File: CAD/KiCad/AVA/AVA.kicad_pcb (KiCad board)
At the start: 2 copper layers, 100 x 75 mm, 48 parts, among them J1 Conn_01x03_Pin, J10 Conn_01x04_Pin, J2 Conn_01x03_Pin, J3 Conn_01x03_Pin, J4 Conn_01x03_Pin, J5 Conn_01x02_Pin, J6 Conn_01x02_Pin, J7 Conn_01x02_Pin, J8 Conn_01x03_Pin, J9 Conn_01x03_Pin, U1 ESP32-C3-Super-Mini, U2 ESP32-DevKitC

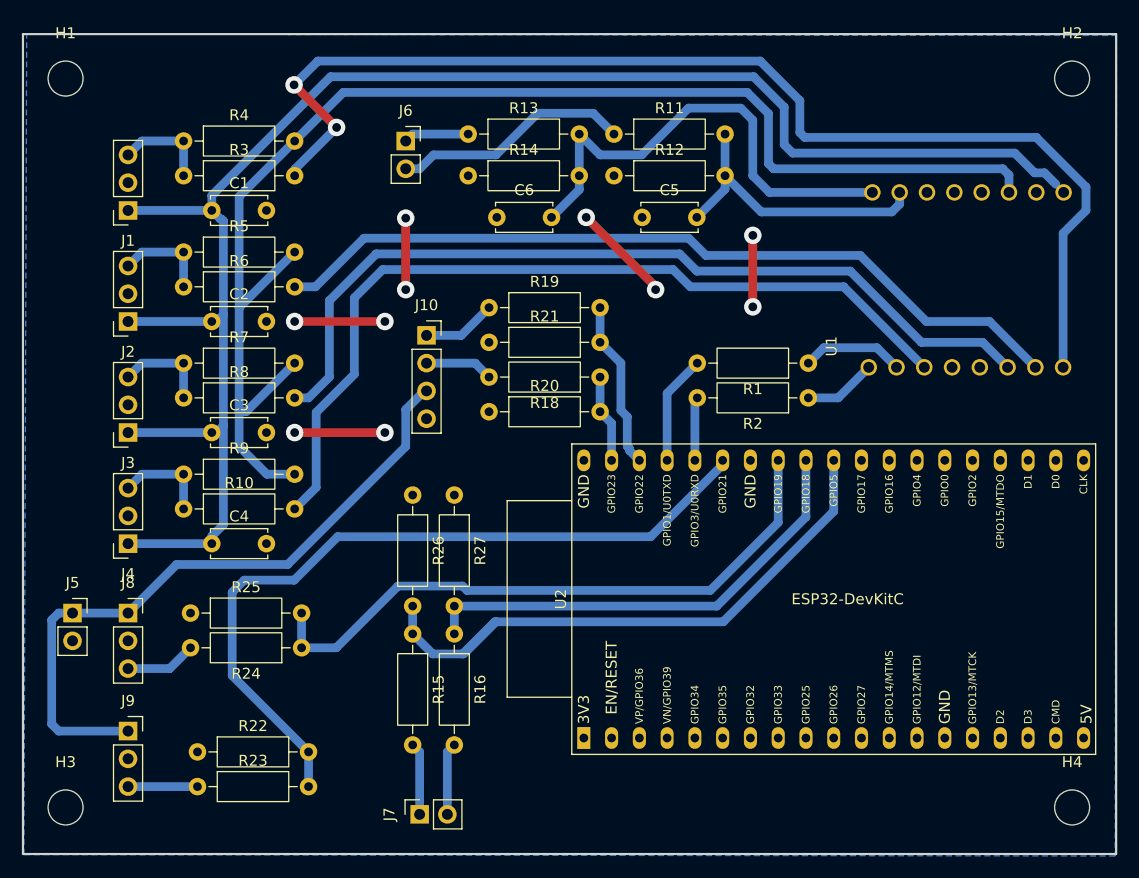
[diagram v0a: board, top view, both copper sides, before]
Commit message: SVG update for connectors
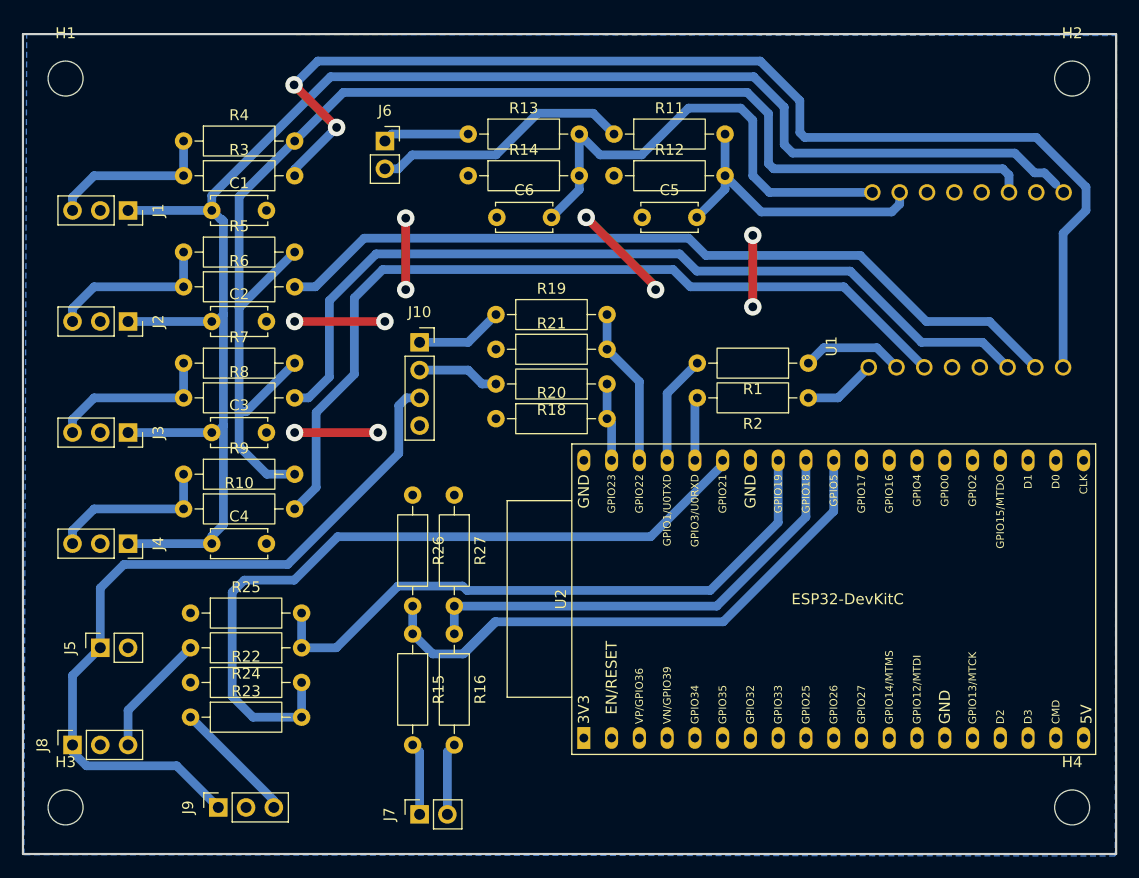
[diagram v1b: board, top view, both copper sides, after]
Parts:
- moved J8 13.1 mm to (131.4, 116.2), turned to 90 degrees
- moved J9 10.8 mm to (144.8, 121.9), turned to 90 degrees
- moved R22 6.38 mm to (142.2, 110.5)
- moved R23 6.38 mm to (142.2, 113.7)
- moved J5 4.07 mm to (134.0, 107.3), turned to 90 degrees
- moved J6 1.91 mm to (160.0, 61.0)
- moved J10 0.90 mm to (163.2, 79.4)
- moved R20 0.90 mm to (170.2, 86.4)
- moved R21 0.90 mm to (170.2, 80.0)
- moved R19 0.90 mm to (170.2, 76.8)
- moved R18 0.90 mm to (180.3, 83.2)
- turned J1 to -90 degrees
- turned J2 to -90 degrees
- turned J3 to -90 degrees
- turned J4 to -90 degrees
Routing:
- net /6.2V: track 61.7 -> 70.5 mm
- net Net-(J4-Pin_3): track 8.78 -> 15.4 mm
- net Net-(J1-Pin_3): track 8.78 -> 15.4 mm
- net Net-(J3-Pin_3): track 8.78 -> 15.4 mm
- net Net-(J2-Pin_3): track 8.78 -> 15.4 mm
- net /PWM-Motor: track 6.35 -> 11.4 mm
- net /PWM-Servo: track 6.50 -> 11.3 mm
- net /BAT2(8V): track 21.9 -> 23.8 mm
- net /BAT1(14V): track 5.98 -> 7.88 mm
- net /CH1: track 6.77 -> 8.04 mm
- net /CH2: track 6.24 -> 7.51 mm
- net Net-(U2-GPIO23): track 8.06 -> 7.16 mm
- net Net-(U2-GPIO22): track 15.5 -> 14.6 mm
- net Net-(U2-GPIO21): track 70.8 -> 69.9 mm
- net GND: track 38.8 -> 38.2 mm

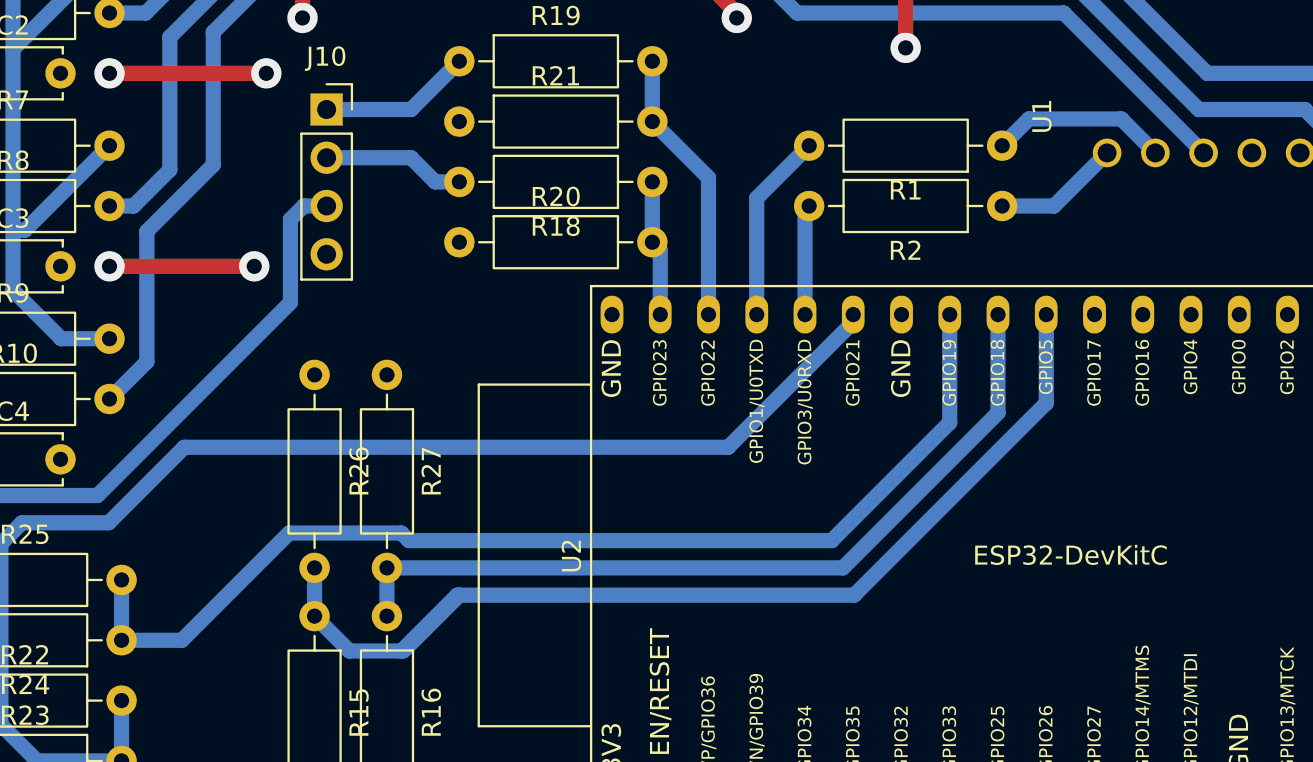
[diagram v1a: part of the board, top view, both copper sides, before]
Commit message: ESP32-DevKitC UART pins shared with usb, changing it to GPIO16/17. GPIO5 is strapping pin, changing pwm channels to GPIO4,18,19,20,21,22,23. GPIO4 in RTC-power-domain (touch sensor for deep-sleep mode, using it as normal PWM GPIO
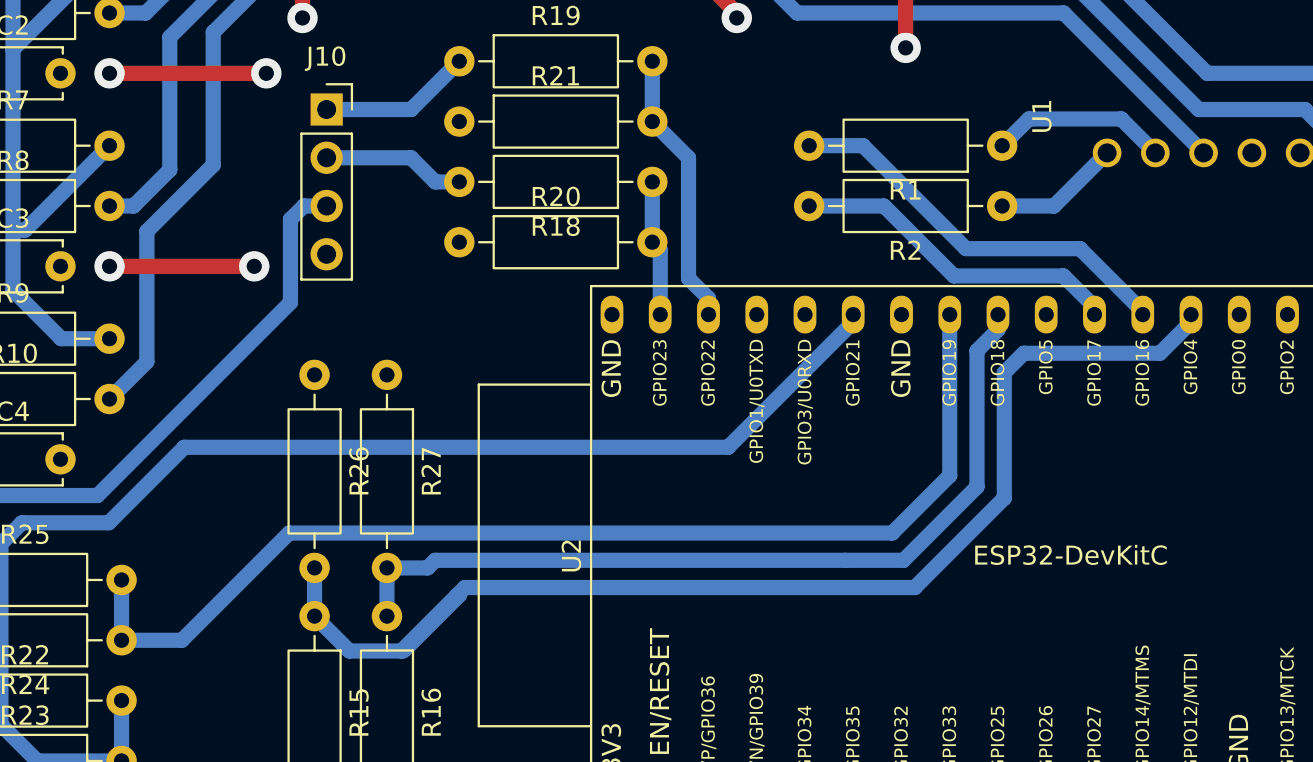
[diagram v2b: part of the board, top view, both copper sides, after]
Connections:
- R1 pad 2: Net-(U2-U0TXD/GPIO1) -> Net-(U2-GPIO16)
- R15 pad 1: Net-(U2-GPIO5) -> Net-(U2-ADC2_CH0/GPIO4)
- R2 pad 2: Net-(U2-U0RXD/GPIO3) -> Net-(U2-GPIO17)
- R26 pad 2: Net-(U2-GPIO5) -> Net-(U2-ADC2_CH0/GPIO4)
- U2 pad 26: unconnected-(U2-ADC2_CH0/GPIO4-Pad26) -> Net-(U2-ADC2_CH0/GPIO4)
- U2 pad 27: unconnected-(U2-GPIO16-Pad27) -> Net-(U2-GPIO16)
- U2 pad 28: unconnected-(U2-GPIO17-Pad28) -> Net-(U2-GPIO17)
- U2 pad 29: Net-(U2-GPIO5) -> unconnected-(U2-GPIO5-Pad29)
- U2 pad 34: Net-(U2-U0RXD/GPIO3) -> unconnected-(U2-U0RXD/GPIO3-Pad34)
- U2 pad 35: Net-(U2-U0TXD/GPIO1) -> unconnected-(U2-U0TXD/GPIO1-Pad35)
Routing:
- net Net-(U2-ADC2_CH0/GPIO4): track 0.00 -> 65.1 mm
- net Net-(U2-GPIO5): track 56.0 -> 0.00 mm
- net Net-(U2-GPIO16): track 0.00 -> 21.3 mm
- net Net-(U2-GPIO17): track 0.00 -> 17.6 mm
- net Net-(U2-U0TXD/GPIO1): track 10.0 -> 0.00 mm
- net Net-(U2-U0RXD/GPIO3): track 5.81 -> 0.00 mm
- net Net-(U2-GPIO18): track 43.3 -> 44.9 mm
- net Net-(U2-GPIO19): track 57.5 -> 58.8 mm

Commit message: Newest SVG, cropped. Footprints I'm flipping, my wrists I'm slitting
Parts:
- U1: moved to B.Cu
- moved R2 14.8 mm to (191.1, 71.8), turned to -90 degrees
- moved R1 10.5 mm to (194.3, 71.8), turned to -90 degrees
- moved U1 4.53 mm to (208.9, 74.5), turned to -90 degrees
- moved C5 2.62 mm to (182.9, 70.5)
- moved J6 2.62 mm to (160.7, 63.5)
- moved R11 2.62 mm to (180.3, 62.9)
- moved R12 2.62 mm to (180.3, 66.7)
- moved C6 2.54 mm to (170.3, 70.5)
- moved R13 2.54 mm to (167.6, 62.9)
- moved R14 2.54 mm to (167.6, 66.7)
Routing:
- net VCC: track 153.9 -> 206.0 mm
- net Net-(U1-3.3V): track 124.9 -> 175.7 mm
- net Net-(U1-PISO/GPIO5): track 108.7 -> 77.5 mm, vias 2 -> 0
- net GND: track 38.2 -> 24.8 mm, vias 10 -> 6
- net Net-(U1-GPIO10): track 78.5 -> 88.1 mm
- net Net-(U1-SS/GPIO7): track 79.1 -> 88.3 mm
- net Net-(U1-POSI/GPIO6): track 74.5 -> 82.0 mm
- net Net-(U1-TX/GPIO21): track 6.68 -> 12.0 mm
- net Net-(U2-GPIO16): track 21.3 -> 16.8 mm
- net Net-(U1-A1/GPIO1): track 27.4 -> 29.8 mm
- net Net-(U1-RX/GPIO20): track 9.39 -> 11.7 mm
- net Net-(U1-A0/GPIO0): track 44.2 -> 42.7 mm
- net /BAT2(8V): track 23.8 -> 22.9 mm
- net /BAT1(14V): track 7.88 -> 7.25 mm
- net Net-(U2-GPIO17): track 17.6 -> 17.1 mm

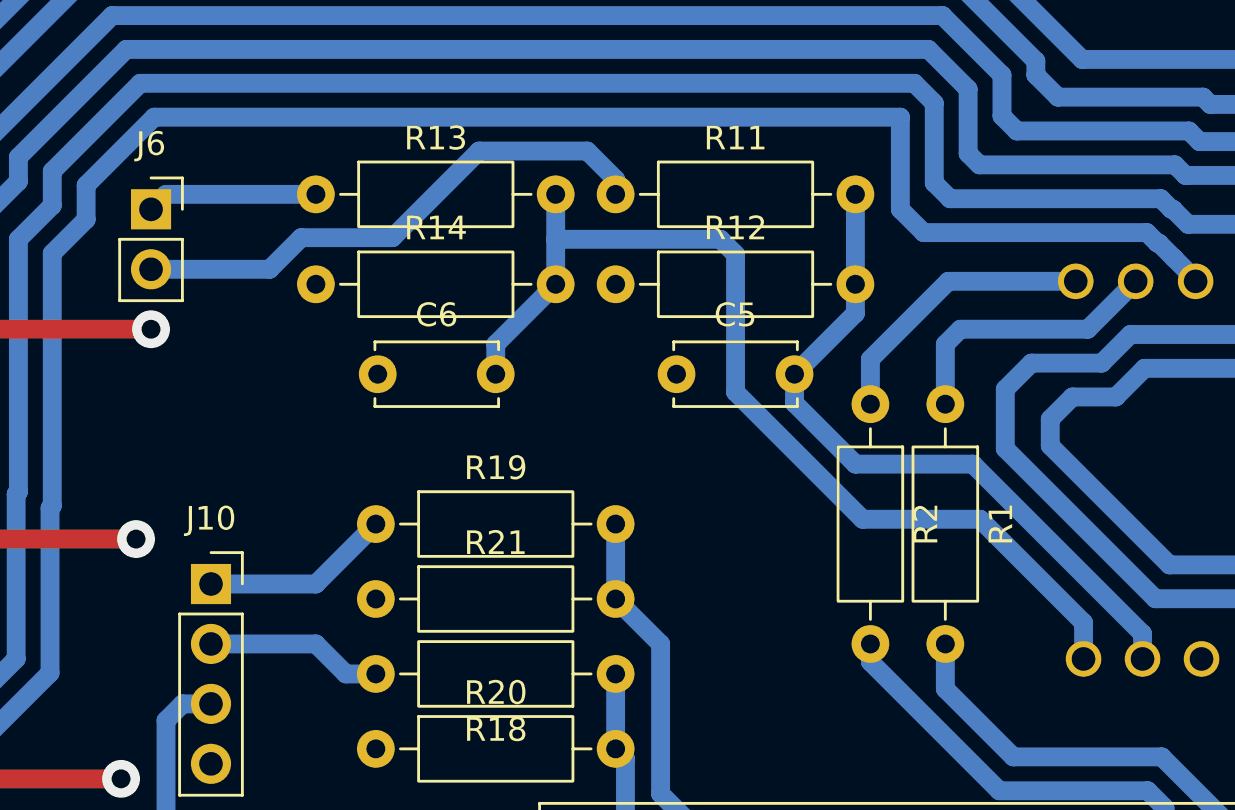
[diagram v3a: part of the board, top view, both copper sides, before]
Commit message: Removed copper islands from circuit
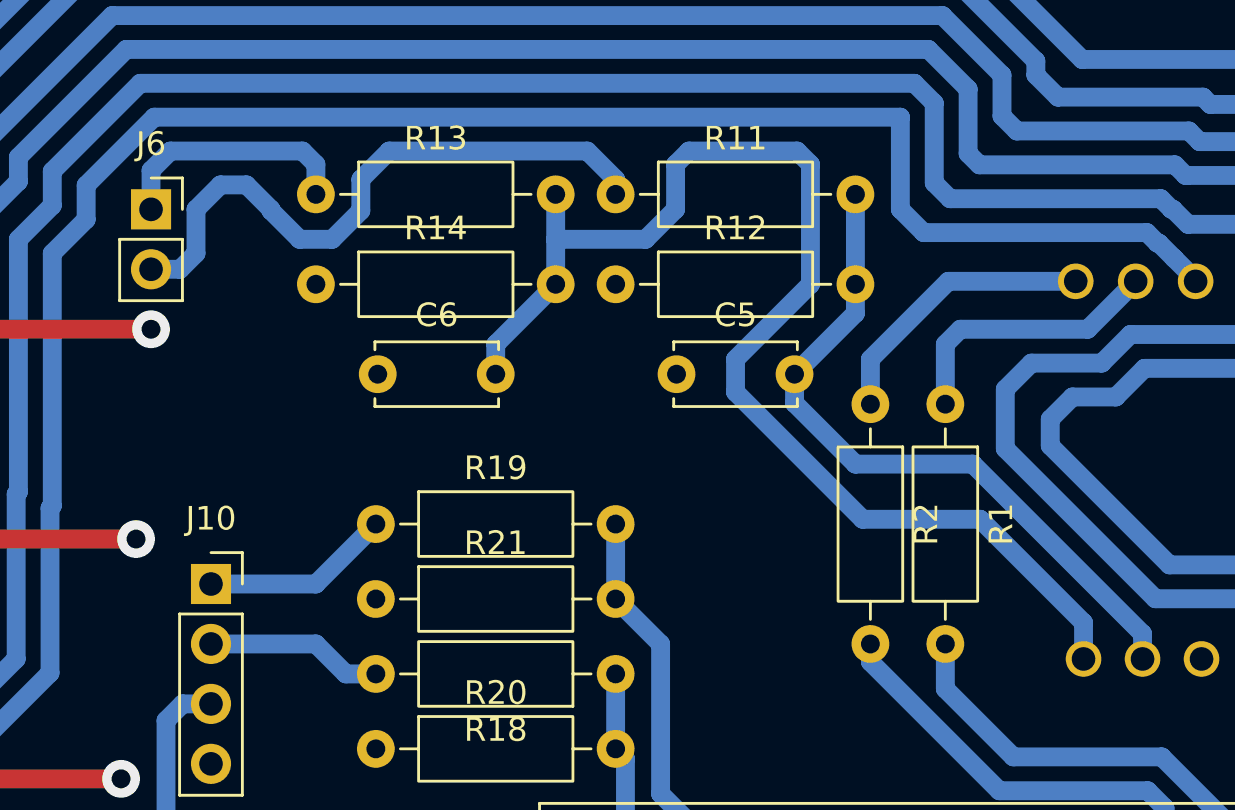
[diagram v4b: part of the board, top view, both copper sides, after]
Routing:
- net Net-(U1-A0/GPIO0): track 42.7 -> 53.7 mm
- net /BAT2(8V): track 22.9 -> 26.7 mm
- net /BAT1(14V): track 7.25 -> 10.5 mm
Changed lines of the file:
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@@
-	)
-	(segment
-		(start 184.785 64.77)
-		(end 177.8 64.77)
-		(width 0.8)
-		(layer "B.Cu")
-		(net "Net-(U1-A0{slash}GPIO0)")
 	)
 	(segment
 		(start 190.807143 76.631539)
+		(end 195.78346 76.631539)
+		(width 0.8)
+		(layer "B.Cu")
+		(net "Net-(U1-A0{slash}GPIO0)")
+	)
+	(segment
+		(start 188.595 66.675)
+		(end 185.42 69.85)
+		(width 0.8)
+		(layer "B.Cu")
+		(net "Net-(U1-A0{slash}GPIO0)")
+	)
+	(segment
+		(start 183.445 61.03)
+		(end 188.03 61.03)
+		(width 0.8)
+		(layer "B.Cu")
+		(net "Net-(U1-A0{slash}GPIO0)")
+	)
+	(segment
+		(start 185.42 69.85)
 		(end 185.42 71.244396)
-		(width 0.8)
-		(layer "B.Cu")
-		(net "Net-(U1-A0{slash}GPIO0)")
-	)
-	(segment
-		(start 185.42 71.244396)
-		(end 185.42 65.405)
-		(width 0.8)
-		(layer "B.Cu")
-		(net "Net-(U1-A0{slash}GPIO0)")
-	)
-	(segment
-		(start 195.78346 76.631539)
-		(end 190.807143 76.631539)
 		(width 0.8)
 		(layer "B.Cu")
@@
 	)
 	(segment
+		(start 182.88 61.595)
+		(end 183.445 61.03)
+		(width 0.8)
+		(layer "B.Cu")
+		(net "Net-(U1-A0{slash}GPIO0)")
+	)
+	(segment
 		(start 177.8 62.865)
 		(end 177.8 64.77)
@@
 	(segment
 		(start 177.8 64.77)
+		(end 181.61 64.77)
+		(width 0.8)
+		(layer "B.Cu")
+		(net "Net-(U1-A0{slash}GPIO0)")
+	)
+	(segment
+		(start 177.8 64.77)
 		(end 177.8 66.675)
 		(width 0.8)
@@
 	)
 	(segment
-		(start 185.42 65.405)
-		(end 184.785 64.77)
-		(width 0.8)
-		(layer "B.Cu")
-		(net "Net-(U1-A0{slash}GPIO0)")
-	)
-	(segment
-		(start 200.165 82.55)
+		(start 185.42 71.244396)
+		(end 190.807143 76.631539)
+		(width 0.8)
+		(layer "B.Cu")
+		(net "Net-(U1-A0{slash}GPIO0)")
+	)
+	(segment
+		(start 181.61 64.77)
+		(end 182.88 63.5)
+		(width 0.8)
+		(layer "B.Cu")
+		(net "Net-(U1-A0{slash}GPIO0)")
+	)
+	(segment
+		(start 188.595 61.595)
+		(end 188.595 66.675)
+		(width 0.8)
+		(layer "B.Cu")
+		(net "Net-(U1-A0{slash}GPIO0)")
+	)
+	(segment
+		(start 182.88 63.5)
+		(end 182.88 61.595)
+		(width 0.8)
+		(layer "B.Cu")
+		(net "Net-(U1-A0{slash}GPIO0)")
+	)
+	(segment
+		(start 200.165 81.013079)
+		(end 200.165 82.55)
+		(width 0.8)
+		(layer "B.Cu")
+		(net "Net-(U1-A0{slash}GPIO0)")
+	)
+	(segment
+		(start 195.78346 76.631539)
 		(end 200.165 81.013079)
 		(width 0.8)
@@
 	)
 	(segment
-		(start 200.165 81.013079)
-		(end 195.78346 76.631539)
+		(start 188.03 61.03)
+		(end 188.595 61.595)
 		(width 0.8)
 		(layer "B.Cu")
@@
 	)
 	(segment
+		(start 191.135 69.85)
+		(end 194.435 66.55)
+		(width 0.8)
+		(layer "B.Cu")
+		(net "Net-(U1-TX{slash}GPIO21)")
+	)
+	(segment
+		(start 191.135 71.755)
+		(end 191.135 69.85)
+		(width 0.8)
+		(layer "B.Cu")
+		(net "Net-(U1-TX{slash}GPIO21)")
+	)
+	(segment
 		(start 194.435 66.55)
 		(end 199.835 66.55)
@@
 	)
 	(segment
-		(start 191.135 71.755)
-		(end 191.135 69.85)
-		(width 0.8)
-		(layer "B.Cu")
-		(net "Net-(U1-TX{slash}GPIO21)")
-	)
-	(segment
-		(start 191.135 69.85)
-		(end 194.435 66.55)
-		(width 0.8)
-		(layer "B.Cu")
-		(net "Net-(U1-TX{slash}GPIO21)")
-	)
-	(segment
 		(start 149.86 121.92)
 		(end 149.86 121.285)
@@
 	)
 	(segment
-		(start 167.64 62.865)
-		(end 161.29 62.865)
+		(start 160.655 61.85)
+		(end 161.475 61.03)
 		(width 0.8)
 		(layer "B.Cu")
@@
 	)
 	(segment
-		(start 161.29 62.865)
-		(end 160.655 63.5)
+		(start 167.075 61.03)
+		(end 167.64 61.595)
+		(width 0.8)
+		(layer "B.Cu")
+		(net "/BAT1(14V)")
+	)
+	(segment
+		(start 167.64 61.595)
+		(end 167.64 62.865)
+		(width 0.8)
+		(layer "B.Cu")
+		(net "/BAT1(14V)")
+	)
+	(segment
+		(start 160.655 63.5)
+		(end 160.655 61.85)
+		(width 0.8)
+		(layer "B.Cu")
+		(net "/BAT1(14V)")
+	)
+	(segment
+		(start 161.475 61.03)
+		(end 167.075 61.03)
 		(width 0.8)
 		(layer "B.Cu")
@@
 	)
 	(segment
-		(start 174.555 61.03)
+		(start 170.745 61.03)
 		(end 179.14 61.03)
 		(width 0.8)
@@
 	)
 	(segment
+		(start 169.545 63.555082)
+		(end 169.545 62.23)
+		(width 0.8)
+		(layer "B.Cu")
+		(net "/BAT2(8V)")
+	)
+	(segment
+		(start 162.56 65.365)
+		(end 162.56 63.5)
+		(width 0.8)
+		(layer "B.Cu")
+		(net "/BAT2(8V)")
+	)
+	(segment
+		(start 164.7 62.465)
+		(end 165.735 63.5)
+		(width 0.8)
+		(layer "B.Cu")
+		(net "/BAT2(8V)")
+	)
+	(segment
+		(start 168.330082 64.77)
+		(end 169.545 63.555082)
+		(width 0.8)
+		(layer "B.Cu")
+		(net "/BAT2(8V)")
+	)
+	(segment
+		(start 165.735 63.5)
+		(end 165.735 63.555082)
+		(width 0.8)
+		(layer "B.Cu")
+		(net "/BAT2(8V)")
+	)
+	(segment
 		(start 160.655 66.04)
-		(end 165.679918 66.04)
-		(width 0.8)
-		(layer "B.Cu")
-		(net "/BAT2(8V)")
-	)
-	(segment
-		(start 170.885 64.7)
-		(end 174.555 61.03)
-		(width 0.8)
-		(layer "B.Cu")
-		(net "/BAT2(8V)")
-	)
-	(segment
-		(start 167.019918 64.7)
-		(end 170.885 64.7)
-		(width 0.8)
-		(layer "B.Cu")
-		(net "/BAT2(8V)")
-	)
-	(segment
-		(start 165.679918 66.04)
-		(end 167.019918 64.7)
+		(end 161.885 66.04)
+		(width 0.8)
+		(layer "B.Cu")
+		(net "/BAT2(8V)")
+	)
+	(segment
+		(start 162.56 63.5)
+		(end 163.595 62.465)
+		(width 0.8)
+		(layer "B.Cu")
+		(net "/BAT2(8V)")
+	)
+	(segment
+		(start 166.949918 64.77)
+		(end 168.330082 64.77)
+		(width 0.8)
+		(layer "B.Cu")
+		(net "/BAT2(8V)")
+	)
+	(segment
+		(start 161.885 66.04)
+		(end 162.56 65.365)
 		(width 0.8)
 		(layer "B.Cu")
@@
 	)
 	(segment
+		(start 163.595 62.465)
+		(end 164.7 62.465)
+		(width 0.8)
+		(layer "B.Cu")
+		(net "/BAT2(8V)")
+	)
+	(segment
 		(start 179.14 61.03)
 		(end 180.34 62.23)
 		(width 0.8)
 		(layer "B.Cu")
+		(net "/BAT2(8V)")
+	)
+	(segment
+		(start 169.545 62.23)
+		(end 170.745 61.03)
+		(width 0.8)
+		(layer "B.Cu")
+		(net "/BAT2(8V)")
+	)
+	(segment
+		(start 165.735 63.555082)
+		(end 166.949918 64.77)
+		(width 0.8)
+		(layer "B.Cu")
